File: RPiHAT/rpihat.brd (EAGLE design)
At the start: 65 x 56.5 mm, 37 parts, among them U1 24LC-I/OT

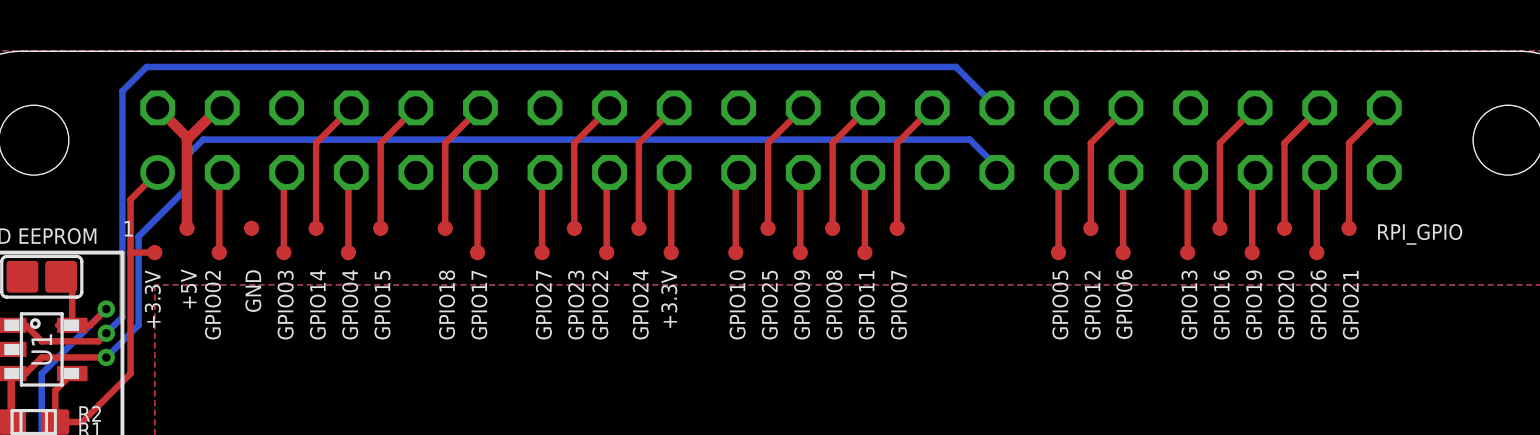
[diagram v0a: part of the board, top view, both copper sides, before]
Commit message: RPi HAT: Center traces between connector pins.
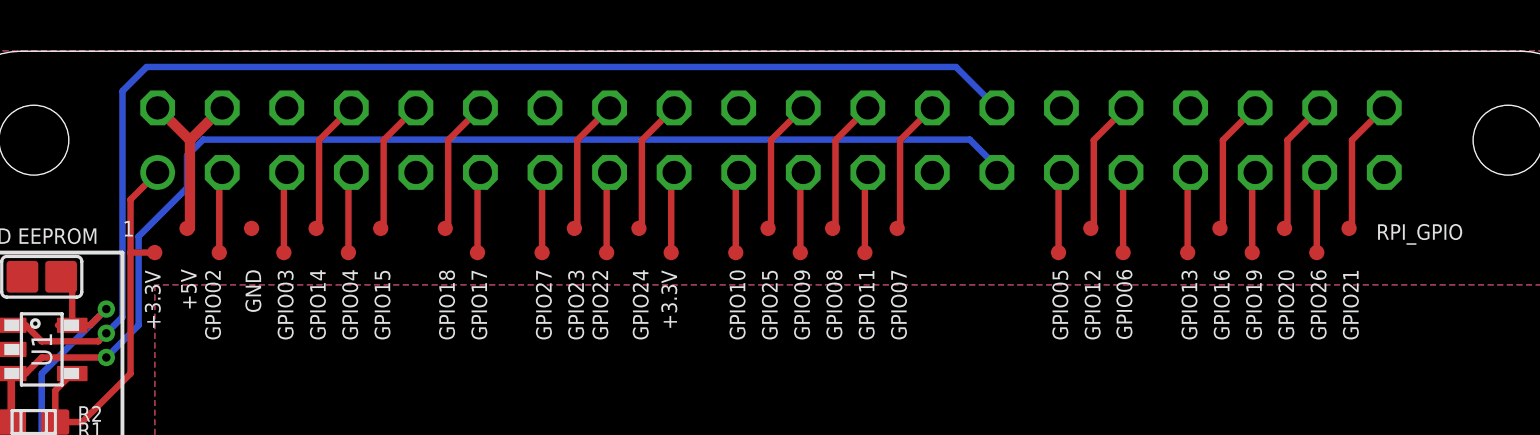
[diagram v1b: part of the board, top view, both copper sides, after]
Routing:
- net +5V: track 10.6 -> 7.34 mm
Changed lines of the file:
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@@
 <?xml version="1.0" encoding="utf-8"?>
 <!DOCTYPE eagle SYSTEM "eagle.dtd">
-<eagle version="7.3.0">
+<eagle version="7.5.0">
 <drawing>
 <settings>
@@
 <setting verticaltext="up"/>
 </settings>
-<grid distance="12.5" unitdist="mil" unit="mil" style="lines" multiple="1" display="no" altdistance="0.025" altunitdist="inch" altunit="inch"/>
+<grid distance="0.025" unitdist="inch" unit="inch" style="lines" multiple="1" display="no" altdistance="0.025" altunitdist="inch" altunit="inch"/>
 <layers>
 <layer number="1" name="Top" color="4" fill="1" visible="yes" active="yes"/>
@@
 <contactref element="RPI_GPIO" pad="40"/>
 <contactref element="GPIO21" pad="TP"/>
-<wire x1="56.63" y1="54.27" x2="55.245" y2="52.885" width="0.254" layer="1"/>
-<wire x1="55.245" y1="52.885" x2="55.245" y2="49.53" width="0.254" layer="1"/>
+<wire x1="56.63" y1="54.27" x2="55.36" y2="53" width="0.254" layer="1"/>
+<wire x1="55.36" y1="53" x2="55.36" y2="49.53" width="0.254" layer="1"/>
+<wire x1="55.36" y1="49.53" x2="55.245" y2="49.415" width="0.254" layer="1"/>
+<wire x1="55.245" y1="49.415" x2="55.245" y2="49.53" width="0.254" layer="1"/>
 </signal>
 <signal name="RPI_GPIO20">
 <contactref element="RPI_GPIO" pad="38"/>
 <contactref element="GPIO20" pad="TP"/>
-<wire x1="52.705" y1="49.53" x2="52.705" y2="52.885" width="0.254" layer="1"/>
-<wire x1="52.705" y1="52.885" x2="54.09" y2="54.27" width="0.254" layer="1"/>
+<wire x1="54.09" y1="54.27" x2="52.82" y2="53" width="0.254" layer="1"/>
+<wire x1="52.82" y1="53" x2="52.82" y2="49.53" width="0.254" layer="1"/>
+<wire x1="52.82" y1="49.53" x2="52.705" y2="49.415" width="0.254" layer="1"/>
+<wire x1="52.705" y1="49.415" x2="52.705" y2="49.53" width="0.254" layer="1"/>
 </signal>
 <signal name="RPI_GPIO16">
 <contactref element="RPI_GPIO" pad="36"/>
 <contactref element="GPIO16" pad="TP"/>
-<wire x1="50.165" y1="49.53" x2="50.165" y2="52.885" width="0.254" layer="1"/>
-<wire x1="50.165" y1="52.885" x2="51.55" y2="54.27" width="0.254" layer="1"/>
+<wire x1="51.55" y1="54.27" x2="50.28" y2="53" width="0.254" layer="1"/>
+<wire x1="50.28" y1="53" x2="50.28" y2="49.53" width="0.254" layer="1"/>
+<wire x1="50.28" y1="49.53" x2="50.165" y2="49.415" width="0.254" layer="1"/>
+<wire x1="50.165" y1="49.415" x2="50.165" y2="49.53" width="0.254" layer="1"/>
 </signal>
 <signal name="RPI_GPIO12">
 <contactref element="RPI_GPIO" pad="32"/>
 <contactref element="GPIO12" pad="TP"/>
-<wire x1="45.085" y1="49.53" x2="45.085" y2="52.885" width="0.254" layer="1"/>
-<wire x1="45.085" y1="52.885" x2="46.47" y2="54.27" width="0.254" layer="1"/>
+<wire x1="46.47" y1="54.27" x2="45.2" y2="53" width="0.254" layer="1"/>
+<wire x1="45.2" y1="53" x2="45.2" y2="49.53" width="0.254" layer="1"/>
+<wire x1="45.2" y1="49.53" x2="45.085" y2="49.415" width="0.254" layer="1"/>
+<wire x1="45.085" y1="49.415" x2="45.085" y2="49.53" width="0.254" layer="1"/>
 </signal>
 <signal name="RPI_GPIO07">
 <contactref element="RPI_GPIO" pad="26"/>
 <contactref element="GPIO07" pad="TP"/>
-<wire x1="37.465" y1="49.53" x2="37.465" y2="52.885" width="0.254" layer="1"/>
-<wire x1="37.465" y1="52.885" x2="38.85" y2="54.27" width="0.254" layer="1"/>
+<wire x1="38.85" y1="54.27" x2="37.58" y2="53" width="0.254" layer="1"/>
+<wire x1="37.58" y1="53" x2="37.58" y2="49.53" width="0.254" layer="1"/>
+<wire x1="37.58" y1="49.53" x2="37.465" y2="49.415" width="0.254" layer="1"/>
+<wire x1="37.465" y1="49.415" x2="37.465" y2="49.53" width="0.254" layer="1"/>
 </signal>
 <signal name="RPI_GPIO08">
 <contactref element="RPI_GPIO" pad="24"/>
 <contactref element="GPIO08" pad="TP"/>
-<wire x1="34.925" y1="49.53" x2="34.925" y2="52.885" width="0.254" layer="1"/>
-<wire x1="34.925" y1="52.885" x2="36.31" y2="54.27" width="0.254" layer="1"/>
+<wire x1="36.31" y1="54.27" x2="35.04" y2="53" width="0.254" layer="1"/>
+<wire x1="35.04" y1="53" x2="35.04" y2="49.53" width="0.254" layer="1"/>
+<wire x1="35.04" y1="49.53" x2="34.925" y2="49.415" width="0.254" layer="1"/>
+<wire x1="34.925" y1="49.415" x2="34.925" y2="49.53" width="0.254" layer="1"/>
 </signal>
 <signal name="RPI_GPIO25">
 <contactref element="RPI_GPIO" pad="22"/>
 <contactref element="GPIO25" pad="TP"/>
-<wire x1="32.385" y1="49.53" x2="32.385" y2="52.885" width="0.254" layer="1"/>
-<wire x1="32.385" y1="52.885" x2="33.77" y2="54.27" width="0.254" layer="1"/>
+<wire x1="33.77" y1="54.27" x2="32.5" y2="53" width="0.254" layer="1"/>
+<wire x1="32.5" y1="53" x2="32.5" y2="49.53" width="0.254" layer="1"/>
+<wire x1="32.5" y1="49.53" x2="32.385" y2="49.415" width="0.254" layer="1"/>
+<wire x1="32.385" y1="49.415" x2="32.385" y2="49.53" width="0.254" layer="1"/>
 </signal>
 <signal name="RPI_GPIO24">
 <contactref element="RPI_GPIO" pad="18"/>
 <contactref element="GPIO24" pad="TP"/>
-<wire x1="27.305" y1="49.53" x2="27.305" y2="52.885" width="0.254" layer="1"/>
-<wire x1="27.305" y1="52.885" x2="28.69" y2="54.27" width="0.254" layer="1"/>
+<wire x1="28.69" y1="54.27" x2="27.42" y2="53" width="0.254" layer="1"/>
+<wire x1="27.42" y1="53" x2="27.42" y2="49.53" width="0.254" layer="1"/>
+<wire x1="27.42" y1="49.53" x2="27.305" y2="49.415" width="0.254" layer="1"/>
+<wire x1="27.305" y1="49.415" x2="27.305" y2="49.53" width="0.254" layer="1"/>
 </signal>
 <signal name="RPI_GPIO23">
 <contactref element="RPI_GPIO" pad="16"/>
 <contactref element="GPIO23" pad="TP"/>
-<wire x1="24.765" y1="49.53" x2="24.765" y2="52.885" width="0.254" layer="1"/>
-<wire x1="24.765" y1="52.885" x2="26.15" y2="54.27" width="0.254" layer="1"/>
+<wire x1="26.15" y1="54.27" x2="24.88" y2="53" width="0.254" layer="1"/>
+<wire x1="24.88" y1="53" x2="24.88" y2="49.53" width="0.254" layer="1"/>
+<wire x1="24.88" y1="49.53" x2="24.765" y2="49.415" width="0.254" layer="1"/>
+<wire x1="24.765" y1="49.415" x2="24.765" y2="49.53" width="0.254" layer="1"/>
 </signal>
 <signal name="RPI_GPIO18">
 <contactref element="RPI_GPIO" pad="12"/>
 <contactref element="GPIO18" pad="TP"/>
-<wire x1="19.685" y1="49.53" x2="19.685" y2="52.885" width="0.254" layer="1"/>
-<wire x1="19.685" y1="52.885" x2="21.07" y2="54.27" width="0.254" layer="1"/>
+<wire x1="21.07" y1="54.27" x2="19.8" y2="53" width="0.254" layer="1"/>
+<wire x1="19.8" y1="53" x2="19.8" y2="49.53" width="0.254" layer="1"/>
+<wire x1="19.8" y1="49.53" x2="19.685" y2="49.415" width="0.254" layer="1"/>
+<wire x1="19.685" y1="49.415" x2="19.685" y2="49.53" width="0.254" layer="1"/>
 </signal>
 <signal name="RPI_GPIO15">
 <contactref element="RPI_GPIO" pad="10"/>
 <contactref element="GPIO15" pad="TP"/>
-<wire x1="17.145" y1="49.53" x2="17.145" y2="52.885" width="0.254" layer="1"/>
-<wire x1="17.145" y1="52.885" x2="18.53" y2="54.27" width="0.254" layer="1"/>
+<wire x1="18.53" y1="54.27" x2="17.26" y2="53" width="0.254" layer="1"/>
+<wire x1="17.26" y1="53" x2="17.26" y2="49.53" width="0.254" layer="1"/>
+<wire x1="17.26" y1="49.53" x2="17.145" y2="49.415" width="0.254" layer="1"/>
+<wire x1="17.145" y1="49.415" x2="17.145" y2="49.53" width="0.254" layer="1"/>
 </signal>
 <signal name="RPI_GPIO14">
 <contactref element="RPI_GPIO" pad="8"/>
 <contactref element="GPIO14" pad="TP"/>
-<wire x1="14.605" y1="49.53" x2="14.605" y2="52.885" width="0.254" layer="1"/>
-<wire x1="14.605" y1="52.885" x2="15.99" y2="54.27" width="0.254" layer="1"/>
+<wire x1="15.99" y1="54.27" x2="14.72" y2="53" width="0.254" layer="1"/>
+<wire x1="14.72" y1="53" x2="14.72" y2="49.53" width="0.254" layer="1"/>
+<wire x1="14.72" y1="49.53" x2="14.605" y2="49.415" width="0.254" layer="1"/>
+<wire x1="14.605" y1="49.415" x2="14.605" y2="49.53" width="0.254" layer="1"/>
 </signal>
 <signal name="+5V">
@@
 <contactref element="RPI_GPIO" pad="2"/>
 <contactref element="+5V" pad="TP"/>
-<wire x1="9.525" y1="53.115" x2="8.37" y2="54.27" width="0.4064" layer="1"/>
-<wire x1="9.525" y1="49.53" x2="9.525" y2="53.115" width="0.4064" layer="1"/>
-<wire x1="9.525" y1="49.53" x2="9.525" y2="53.0225" width="0.4064" layer="1"/>
-<wire x1="9.525" y1="53.0225" x2="10.7725" y2="54.27" width="0.4064" layer="1"/>
-<wire x1="10.7725" y1="54.27" x2="10.91" y2="54.27" width="0.4064" layer="1"/>
+<wire x1="10.91" y1="54.27" x2="9.64" y2="53" width="0.4064" layer="1"/>
+<wire x1="9.64" y1="53" x2="9.64" y2="49.53" width="0.4064" layer="1"/>
+<wire x1="9.64" y1="49.53" x2="9.525" y2="49.415" width="0.254" layer="1"/>
+<wire x1="9.525" y1="49.415" x2="9.525" y2="49.53" width="0.254" layer="1"/>
+<wire x1="8.37" y1="54.27" x2="9.64" y2="53" width="0.4064" layer="1"/>
 </signal>
 <signal name="RPI_GPIO02">
